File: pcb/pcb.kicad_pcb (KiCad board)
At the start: 2 copper layers, 46 parts, among them J1 Dubugging Headers, J2 Dubugging Headers, SW1 Cherry MX Grey Switch w/ Gree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, SW2 Cherry MX Grey Switch w/ Gree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, SW3 1241.1100.7095, SW4 SW_SPST, U1 Display Driver, U2 Display Driver, U3 MCU, U4 Inverter, 3 Channels, U5 3:8 Demux, U6 NOR, 4 Channels, U7 OR, 2 Channels, U8 5V Buck Voltage Regulator, Y1 20MHz Crystal

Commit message: begin split pcb layout
Signed-off-by: Michael Darr <michael.e.darr@gmail.com>
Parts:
- added C15: 0.1µF, chess_clock:RDER71H104K0M1H03A, F.Cu at (300.2, 42.8)
- added D2: TVS Diode, Diode_SMD:D_SOD-523, F.Cu at (127.3, 205.8)
- added R10: 4.7kΩ, Resistor_THT:R_Axial_DIN0204_L3.6mm_D1.6mm_P2.54mm_Vertical, F.Cu at (285.7, 57.1)
- added R9: 50Ω, chess_clock:352151RFT, F.Cu at (288.5, 49.0)
- J1: value Dubugging Headers -> Debugging; footprint chess_clock:10129381-916001BLF -> Connector_PinHeader_2.54mm:PinHeader_2x16_P2.54mm_Vertical
- J2: value Dubugging Headers -> ISP; footprint chess_clock:10129381-916001BLF -> Connector_PinHeader_2.54mm:PinHeader_2x03_P2.54mm_Vertical
- Y1: value 20MHz Crystal -> 20MHz
- moved U1 233.3 mm to (85.9, 258.7), turned to 90 degrees
- moved C1 198.6 mm to (81.5, 256.2), turned to -90 degrees
- moved U2 193.6 mm to (181.6, 258.7), turned to 90 degrees
- moved R1 187.7 mm to (96.1, 219.3), turned to 180 degrees
- moved R6 173.8 mm to (94.9, 195.0)
- moved SW1 171.7 mm to (92.3, 207.2)
- moved LCD1 151.1 mm to (110.2, 250.8), turned to 90 degrees
- moved LCD2 139.7 mm to (205.8, 250.8), turned to 90 degrees
- moved C7 137.1 mm to (110.5, 210.6), turned to 180 degrees
- moved U3 136.1 mm to (132.5, 205.1)
- moved C2 134.3 mm to (176.8, 256.2), turned to -90 degrees
- moved J1 133.7 mm to (219.7, 16.5)
- moved J2 132.5 mm to (219.7, 24.1)
- moved C3 119.3 mm to (132.5, 198.7), turned to 180 degrees
- moved C14 115.6 mm to (117.3, 205.1), turned to -90 degrees
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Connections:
- C10 pad 2: Net-(BT1-+) -> Net-(U8-VIN)
- C9 pad 1: Net-(BT1-+) -> Net-(U8-VIN)
- J1 pad 10: GND -> digit_2
- J1 pad 11: GND -> digit_1
- J1 pad 12: GND -> data_3
- J1 pad 13: GND -> data_2
- J1 pad 14: GND -> data_1
- J1 pad 15: GND -> data_0
- J1 pad 16: GND -> VCC
- U8 pad 7: Net-(BT1-+) -> Net-(U8-VIN)
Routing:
- net bp: track 0.00 -> 444.6 mm, vias 0 -> 2
- net mux_b: track 0.00 -> 222.0 mm, vias 0 -> 1
- net VCC: track 0.00 -> 218.5 mm, vias 0 -> 1
- net data_0: track 0.00 -> 158.2 mm, vias 0 -> 1
- net data_1: track 0.00 -> 155.1 mm, vias 0 -> 1
- net data_3: track 0.00 -> 154.3 mm, vias 0 -> 1
- net data_2: track 0.00 -> 151.9 mm, vias 0 -> 1
- net digit_1: track 0.00 -> 151.7 mm, vias 0 -> 1
- net digit_2: track 0.00 -> 149.9 mm, vias 0 -> 1
- net /led_1: track 0.00 -> 146.6 mm
- net ~{bp}: track 0.00 -> 128.3 mm, vias 0 -> 1
- net col1: track 0.00 -> 111.0 mm, vias 0 -> 2
- net cs_1_1: track 0.00 -> 109.0 mm, vias 0 -> 1
- net cs_1_2: track 0.00 -> 101.7 mm, vias 0 -> 1
- net /LCD1.G2: track 0.00 -> 90.8 mm
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
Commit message: Separate board halves
Signed-off-by: Michael Darr <michael.e.darr@gmail.com>
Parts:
- moved C6 178.7 mm to (177.1, 206.7)
- moved FET2 140.3 mm to (186.3, 194.5)
- moved C7 82.9 mm to (193.0, 202.6), turned to -90 degrees
- moved U7 77.6 mm to (188.1, 200.9)
- moved U6 76.8 mm to (177.0, 200.1), turned to 180 degrees
- moved C11 57.7 mm to (185.2, 69.7)
- moved C12 57.7 mm to (174.3, 70.2)
- moved C15 57.7 mm to (244.2, 56.4)
- moved C9 57.7 mm to (174.3, 64.3)
- moved J2 57.7 mm to (163.7, 37.8)
- moved LED1 57.7 mm to (110.1, 74.5)
- moved R4 57.7 mm to (210.8, 42.3)
- moved R5 57.7 mm to (210.8, 45.4)
- moved R9 57.7 mm to (232.5, 62.7)
- moved U8 57.7 mm to (130.0, 71.9)
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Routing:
- net ~{col1_enable}: track 2.74 -> 162.6 mm
- net data_3: track 154.3 -> 243.7 mm, vias 1 -> 2
- net ~{sw2_enable}: track 0.00 -> 37.7 mm
- net Net-(FET2-G): track 0.00 -> 36.9 mm
- net ~{bp}: track 128.3 -> 163.2 mm, vias 1 -> 2
- net buzz: track 25.4 -> 56.6 mm
- net GND: track 25.5 -> 0.00 mm
- net cs_1_1: track 109.0 -> 134.0 mm
- net /led_1: track 146.6 -> 170.9 mm
- net ~{sw1_enable}: track 0.00 -> 18.4 mm
- net VCC: track 218.5 -> 235.8 mm
- net col1: track 111.0 -> 127.4 mm
- net ~{sw3_enable}: track 0.00 -> 14.9 mm
- net /sw1∨2_active: track 0.00 -> 12.7 mm
- net sw1_active: track 0.00 -> 11.6 mm
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
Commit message: Finish basic pcb layout
Signed-off-by: Michael Darr <michael.e.darr@gmail.com>
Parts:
- removed J1: Debugging, Connector_PinHeader_2.54mm:PinHeader_2x16_P2.54mm_Vertical
- C1, C10, C11, C15, C2, C3, C4, C5, C6, C7, C8: footprint chess_clock:RDER71H104K0M1H03A -> chess_clock:GRM033R60J104KE19D
- moved R3 180.4 mm to (40.0, 97.3), turned to -90 degrees
- moved R9 175.6 mm to (65.0, 115.3), turned to 90 degrees
- moved R4 175.2 mm to (45.2, 99.8), turned to 90 degrees
- moved FET1 171.3 mm to (36.7, 104.8)
- moved C15 168.0 mm to (89.7, 122.3), turned to 180 degrees
- moved R5 158.6 mm to (72.0, 122.2), turned to 180 degrees
- moved R1 121.2 mm to (47.2, 108.4), turned to 90 degrees
- moved R2 120.1 mm to (154.4, 120.5)
- moved C4 118.6 mm to (134.5, 107.0), turned to 0 degrees
- moved LCD1 116.8 mm to (54.8, 148.0)
- moved LCD2 116.8 mm to (150.5, 148.0)
- moved U1 116.8 mm to (30.6, 155.9)
- moved U2 116.8 mm to (126.2, 155.9)
- moved C7 114.3 mm to (136.0, 103.6)
- moved C12 112.7 mm to (67.5, 106.0), turned to 180 degrees
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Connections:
- net buzz renamed /buzz
- net mux_a renamed /mux_a
- C1 pad 2: VCC -> GND
- C10 pad 1: GND -> Net-(J2-GND)
- C12 pad 1: VCC -> GND
- C2 pad 2: VCC -> GND
- C3 pad 2: VCC -> GND
- C4 pad 1: VCC -> GND
- C5 pad 1: VCC -> GND
- C6 pad 1: VCC -> GND
- C7 pad 1: VCC -> GND
- C7 pad 2: GND -> Net-(J2-GND)
- C9 pad 2: GND -> Net-(J2-GND)
- D2 pad 1: VCC -> GND
- FET1 pad 3: VCC -> GND
- J2 pad 2: VCC -> GND
- J2 pad 6: GND -> Net-(J2-GND)
- L1 pad 1: VCC -> GND
- R10 pad 1: VCC -> GND
- R6 pad 2: VCC -> GND
- R7 pad 2: VCC -> GND
- R8 pad 2: VCC -> GND
- SW3 pad 2: GND -> Net-(J2-GND)
- SW4 pad 1: GND -> Net-(J2-GND)
- U1 pad 1: VCC -> GND
- U2 pad 1: VCC -> GND
- U3 pad 1: VCC -> GND
- U4 pad 8: VCC -> GND
- U5 pad 16: VCC -> GND
- U5 pad 6: VCC -> GND
- U6 pad 14: VCC -> GND
- U6 pad 3: VCC -> GND
- U6 pad 5: VCC -> GND
- U6 pad 9: VCC -> GND
- U7 pad 4: GND -> Net-(J2-GND)
- U7 pad 8: VCC -> GND
- U8 pad 4: VCC -> GND
- U8 pad 5: GND -> Net-(J2-GND)
- U8 pad 6: GND -> Net-(J2-GND)
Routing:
- net GND: track 0.00 -> 574.1 mm, vias 0 -> 5
- net VCC: track 235.8 -> 0.00 mm, vias 1 -> 0
- net Net-(SW1-A): track 7.00 -> 85.4 mm
- net Net-(J2-GND): track 0.00 -> 77.9 mm, vias 0 -> 2
- net Net-(D1-K): track 0.00 -> 72.2 mm
- net Net-(BT1-+): track 0.00 -> 68.9 mm
- net Net-(U8-VIN): track 0.00 -> 58.4 mm
- net Net-(FET1-G): track 0.00 -> 54.7 mm
- net ~{col1_enable}: track 162.6 -> 210.4 mm, vias 0 -> 1
- net Net-(R6-Pad1): track 7.14 -> 49.7 mm
- net /buzz: track 56.6 -> 87.8 mm
- net ~{sw3_enable}: track 14.9 -> 38.7 mm
- net mux_b: track 217.4 -> 193.7 mm
- net Net-(U8-VD): track 0.00 -> 23.1 mm
- net Net-(BT1--): track 0.00 -> 22.6 mm
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
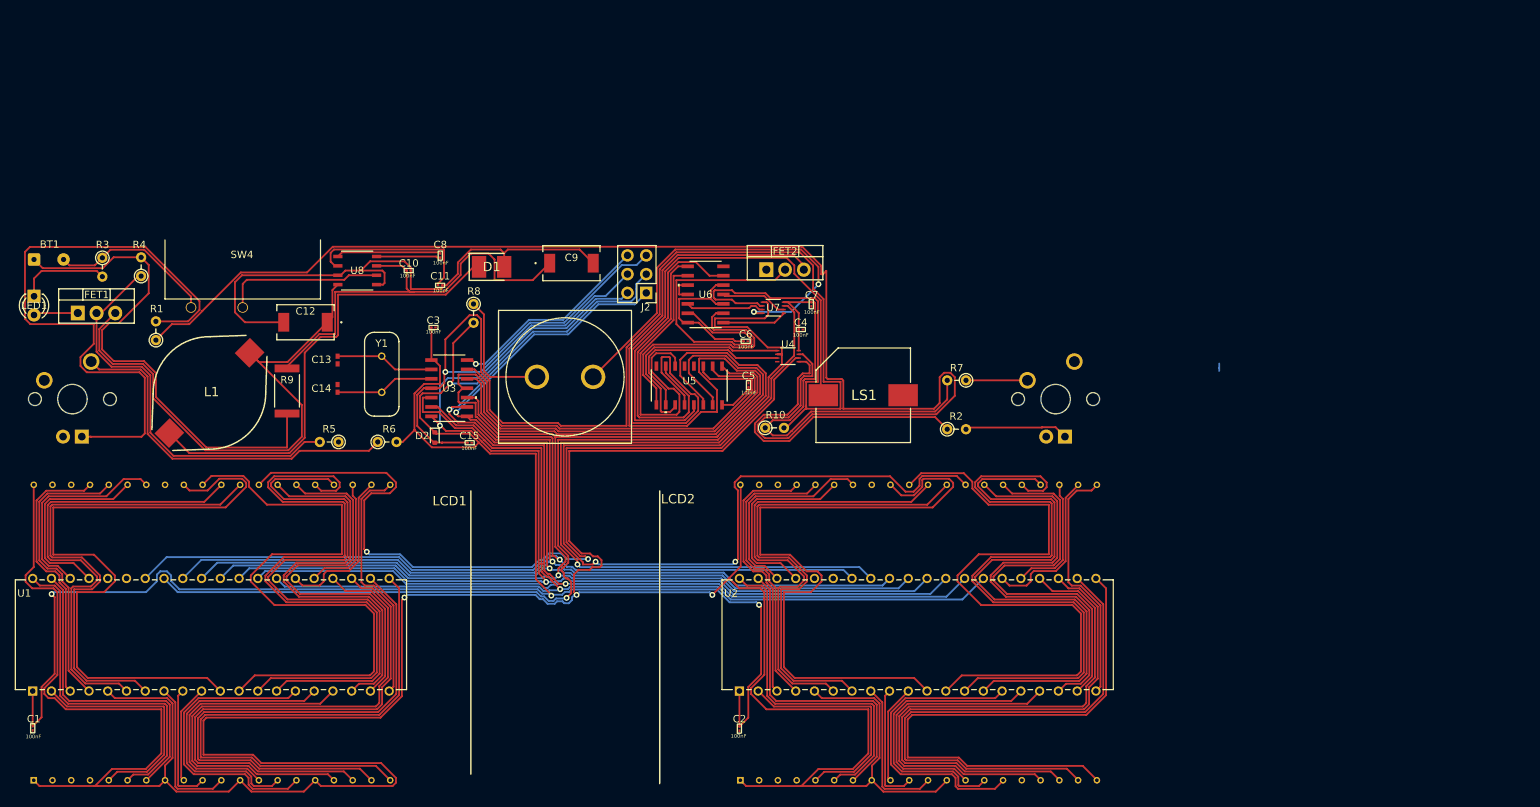
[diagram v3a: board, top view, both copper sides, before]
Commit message: solve solder mask errors
Signed-off-by: Michael Darr <michael.e.darr@gmail.com>
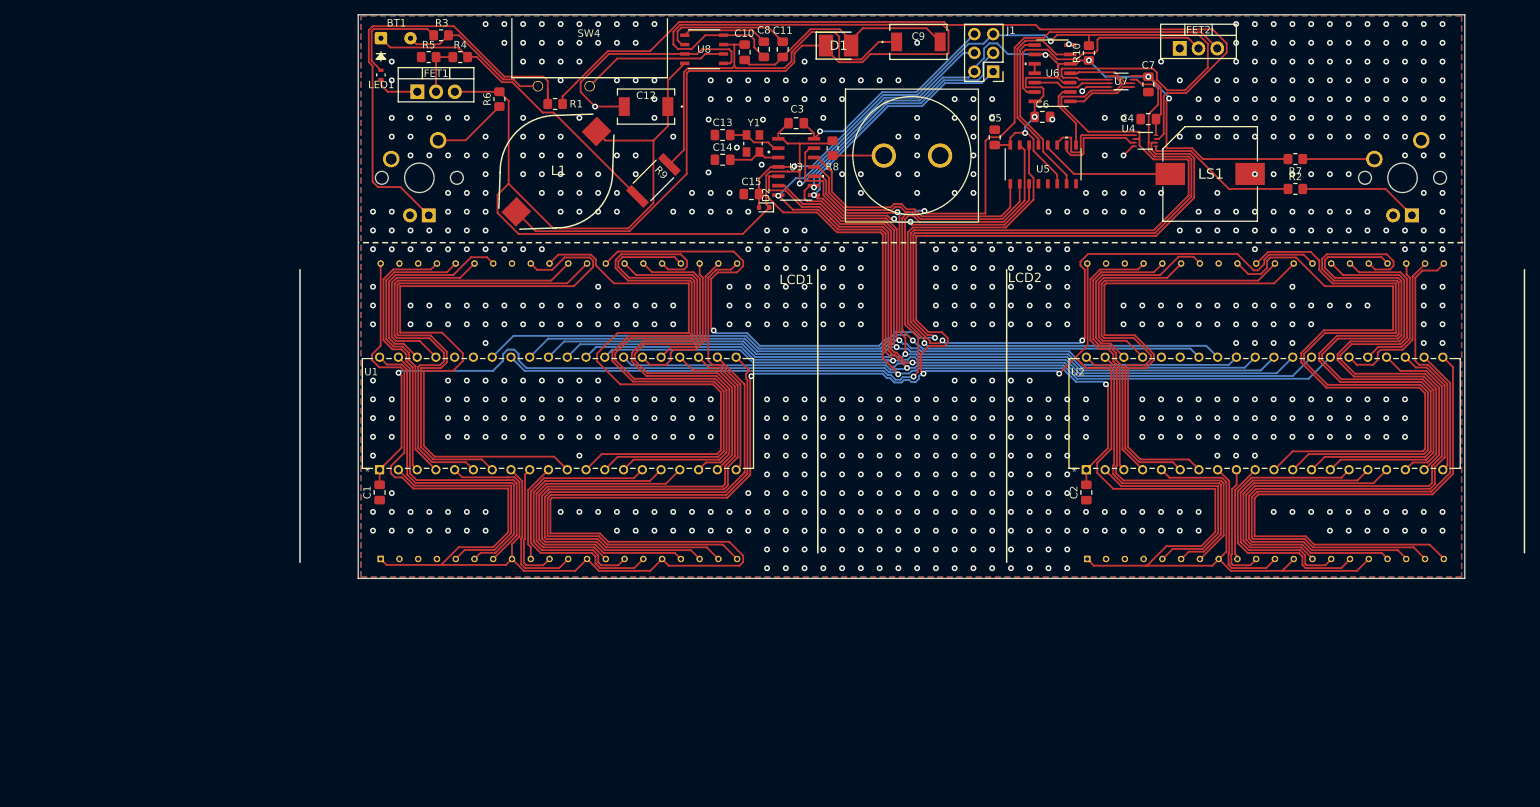
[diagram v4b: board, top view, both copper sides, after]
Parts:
- removed J2: ISP, Connector_PinHeader_2.54mm:PinHeader_2x03_P2.54mm_Vertical
- added J1: ISP, Connector_PinHeader_2.54mm:PinHeader_2x03_P2.54mm_Vertical, F.Cu at (160.6, 72.1)
- C1, C10, C11, C15, C2, C3, C4, C5, C6, C7, C8: footprint chess_clock:GRM033R60J104KE19D -> Capacitor_SMD:C_0805_2012Metric_Pad1.18x1.45mm_HandSolder
- C13, C14: value 11pF -> 22pF; footprint chess_clock:GJM1555C1H110FB01D -> Capacitor_SMD:C_0805_2012Metric_Pad1.18x1.45mm_HandSolder
- LED1: footprint LED_THT:LED_D3.0mm_Clear -> chess_clock:150060RS75000
- R1, R10, R2, R3, R4, R5, R6, R7, R8: footprint Resistor_THT:R_Axial_DIN0204_L3.6mm_D1.6mm_P2.54mm_Vertical -> Resistor_SMD:R_0805_2012Metric_Pad1.20x1.40mm_HandSolder
- Y1: footprint chess_clock:ECS_200_18_4X_CKM -> chess_clock:ABM8-20.000MHZ-10-B1U-T
- moved R10 67.0 mm to (173.6, 69.5), turned to 90 degrees
- moved FET2 63.5 mm to (185.8, 68.9)
- moved R1 62.8 mm to (101.3, 76.5), turned to 180 degrees
- moved C14 60.6 mm to (124.0, 84.0), turned to 0 degrees
- moved C13 60.4 mm to (124.0, 80.7), turned to 0 degrees
- moved Y1 59.2 mm to (128.1, 81.8), turned to 180 degrees
- moved R2 57.3 mm to (201.5, 88.0)
- moved R9 57.2 mm to (114.6, 86.8), turned to 45 degrees
- moved C2 56.8 mm to (173.2, 129.0)
- moved C1 56.8 mm to (77.5, 129.0)
- moved U5 56.5 mm to (167.4, 84.6), turned to 90 degrees
- moved U4 56.5 mm to (181.2, 81.4)
- moved C3 56.3 mm to (133.9, 79.0)
- moved C11 56.3 mm to (132.1, 69.1), turned to 90 degrees
- moved U7 56.2 mm to (177.9, 73.4)
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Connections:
- C1 pad 2: GND -> VCC
- C10 pad 1: Net-(J2-GND) -> GND
- C12 pad 1: GND -> VCC
- C2 pad 2: GND -> VCC
- C3 pad 2: GND -> VCC
- C4 pad 1: GND -> VCC
- C5 pad 1: GND -> VCC
- C6 pad 1: GND -> VCC
- C7 pad 1: GND -> VCC
- C7 pad 2: Net-(J2-GND) -> GND
- C9 pad 2: Net-(J2-GND) -> GND
- D2 pad 1: GND -> VCC
- FET1 pad 3: GND -> VCC
- L1 pad 1: GND -> VCC
- R10 pad 1: GND -> VCC
- R6 pad 2: GND -> VCC
- R7 pad 2: GND -> VCC
- R8 pad 2: GND -> VCC
- SW3 pad 2: Net-(J2-GND) -> GND
- SW4 pad 1: Net-(J2-GND) -> GND
- U1 pad 1: GND -> VCC
- U2 pad 1: GND -> VCC
- U3 pad 1: GND -> VCC
- U4 pad 8: GND -> VCC
- U5 pad 16: GND -> VCC
- U5 pad 6: GND -> VCC
- U6 pad 14: GND -> VCC
- U6 pad 3: GND -> VCC
- U6 pad 5: GND -> VCC
- U6 pad 9: GND -> VCC
- U7 pad 4: Net-(J2-GND) -> GND
- U7 pad 8: GND -> VCC
- U8 pad 4: GND -> VCC
- U8 pad 5: Net-(J2-GND) -> GND
- U8 pad 6: Net-(J2-GND) -> GND
- Y1 pad 2: Net-(U3-(PCINT8/XTAL1/CLKI)_PB0) -> GND
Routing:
- net GND: track 574.1 -> 119.3 mm, vias 5 -> 816
- net VCC: track 0.00 -> 443.8 mm, vias 0 -> 10
- net ~{col1_enable}: track 210.4 -> 109.2 mm, vias 1 -> 2
- net Net-(J2-GND): track 77.9 -> 0.00 mm, vias 2 -> 0
- net /led_1: track 187.7 -> 115.0 mm
- net /buzz: track 87.8 -> 18.4 mm
- net Net-(D1-K): track 72.2 -> 138.3 mm
- net Net-(FET1-G): track 54.7 -> 6.97 mm
- net data_3: track 241.2 -> 200.0 mm, vias 1 -> 3
- net mux_b: track 193.7 -> 153.7 mm
- net Net-(R6-Pad1): track 49.7 -> 10.2 mm
- net cs_1_2: track 111.8 -> 82.9 mm
- net bp: track 441.2 -> 469.0 mm
- net cs_1_1: track 131.1 -> 104.0 mm
- net Net-(BT1-+): track 68.9 -> 43.3 mm
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- added copper zone on B.Cu, net GND
- added copper zone on F.Cu, net GND
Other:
- board outline added: 149.8 x 76.3 mm
- rule pad_to_mask_clearance: 2 -> 0.038
- board text added: "0.1.0"

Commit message: Prepare for connection
Signed-off-by: Michael Darr <michael.e.darr@gmail.com>
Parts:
- added J2: Ribbon Cable Header, chess_clock:903250014, F.Cu at (148.5, 152.5)
- added J3: ISP, Connector_PinHeader_2.54mm:PinHeader_2x03_P2.54mm_Vertical, F.Cu at (160.6, 72.1)
- J1: value ISP -> Ribbon Cable Header; footprint Connector_PinHeader_2.54mm:PinHeader_2x03_P2.54mm_Vertical -> chess_clock:903250014
- moved J1 96.3 mm to (254.9, 91.5)
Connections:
- J1 pad 1: digit_2 -> col1
- J1 pad 2: VCC -> ~{bp}
- J1 pad 3: digit_1 -> cs_1_2
- J1 pad 4: data_2 -> mux_b
- J1 pad 5: ~{col1_enable} -> digit_2
- J1 pad 6: GND -> digit_1

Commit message: crush every error
Signed-off-by: Michael Darr <michael.e.darr@gmail.com>
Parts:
- SW1, SW2: value Cherry MX Grey Switch w/ Green LED -> MX Grey w/ LED
- moved J1 84.1 mm to (170.8, 89.9)
- moved J2 54.8 mm to (148.7, 97.7)
- moved J3 4.57 mm to (156.5, 70.0)
- moved C9 3.89 mm to (147.1, 66.0)
- moved R9 3.70 mm to (114.6, 83.1), turned to 0 degrees
- moved D1 2.14 mm to (138.9, 66.5)
- moved BT1 2.00 mm to (77.7, 65.5)
- moved C10 2.00 mm to (127.0, 67.5)
- moved C11 2.00 mm to (132.1, 67.1)
- moved C13 2.00 mm to (124.0, 78.7)
- moved C14 2.00 mm to (124.0, 82.0)
- moved C15 2.00 mm to (127.9, 86.7)
- moved C3 2.00 mm to (133.9, 77.0)
- moved C4 2.00 mm to (181.6, 76.5)
- moved C5 2.00 mm to (160.8, 79.0)
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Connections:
- C1 pad 1: GND -> VSS
- C1 pad 2: VCC -> VDD
- C2 pad 1: GND -> VSS
- C2 pad 2: VCC -> VDD
- J1 pad 1: col1 -> col1_bp
- J1 pad 11: VCC -> lcd_bp
- J1 pad 12: cs_1_1 -> lcd2_write
- J1 pad 13: bp -> GND
- J1 pad 14: GND -> ~{lcd_bp}
- J1 pad 2: ~{bp} -> VCC
- J1 pad 3: cs_1_2 -> mux_b
- J1 pad 4: mux_b -> lcd1_write
- J2 pad 10: data_0 -> d0
- J2 pad 11: VCC -> bp
- J2 pad 12: cs_1_1 -> cs_1_2
- J2 pad 13: bp -> VSS
- J2 pad 14: GND -> ~{bp}
- J2 pad 2: ~{bp} -> VDD
- J2 pad 3: cs_1_2 -> cs_2
- J2 pad 4: mux_b -> cs_1_1
- J2 pad 5: digit_2 -> ds_2
- J2 pad 6: digit_1 -> ds_1
- J2 pad 7: data_3 -> d3
- J2 pad 8: data_2 -> d2
- J2 pad 9: data_1 -> d1
- U1 pad 1: VCC -> VDD
- U1 pad 27: data_0 -> d0
- U1 pad 28: data_1 -> d1
- U1 pad 29: data_2 -> d2
- U1 pad 30: data_3 -> d3
- U1 pad 31: digit_1 -> ds_1
- U1 pad 32: digit_2 -> ds_2
- U1 pad 34: mux_b -> cs_2
- U1 pad 35: GND -> VSS
- U2 pad 1: VCC -> VDD
- U2 pad 27: data_0 -> d0
- U2 pad 28: data_1 -> d1
- U2 pad 29: data_2 -> d2
- U2 pad 30: data_3 -> d3
- U2 pad 31: digit_1 -> ds_1
- U2 pad 32: digit_2 -> ds_2
- U2 pad 34: mux_b -> cs_2
- U2 pad 35: GND -> VSS
- U2 pad 36: GND -> VSS
- U4 pad 2: ~{bp} -> ~{lcd_bp}
- U4 pad 6: bp -> lcd_bp
- U5 pad 14: cs_1_2 -> lcd2_write
- U5 pad 15: cs_1_1 -> lcd1_write
- U7 pad 1: ~{bp} -> ~{lcd_bp}
- U7 pad 7: col1 -> col1_bp
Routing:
- net VDD: track 0.00 -> 173.2 mm
- net VCC: track 443.8 -> 276.5 mm, vias 10 -> 9
- net ~{bp}: track 161.3 -> 47.5 mm, vias 2 -> 0
- net d0: track 0.00 -> 111.2 mm
- net d2: track 0.00 -> 110.8 mm
- net ds_1: track 0.00 -> 110.8 mm
- net d1: track 0.00 -> 105.6 mm
- net d3: track 0.00 -> 105.6 mm
- net ds_2: track 0.00 -> 105.4 mm
- net cs_2: track 0.00 -> 105.4 mm
- net col1: track 144.1 -> 38.8 mm, vias 2 -> 0
- net mux_b: track 153.7 -> 49.1 mm, vias 1 -> 0
- net data_0: track 139.8 -> 43.7 mm, vias 1 -> 0
- net data_1: track 136.6 -> 41.2 mm, vias 1 -> 0
- net data_2: track 167.9 -> 72.6 mm, vias 2 -> 1
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- added copper zone on B.Cu, net VSS
- added copper zone on F.Cu, net VSS
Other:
- board size 149.8 x 76.3 mm -> 149.7 x 78 mm

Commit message: Add some snazy art
Signed-off-by: Michael Darr <michael.e.darr@gmail.com>
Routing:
- net Net-(SW1-A): track 62.6 -> 60.6 mm
- net /LCD2.A2: track 99.9 -> 99.4 mm
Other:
- board text added: "liclock"
- board text added: "╔════════╗ ║ ║ ╚════════╝ ┏━⬓━━▬━━⬓━ ┌─────┚ ▝███▖▜██▙ │╲ ┗━━━━━━━━━━┛ │ ╒═════╤═══════════╕ │╲│ REV │ 0.1.0 │ │ ├─────┼───────────┤ ╵╲│ MFR │ JLCPCB │ ├─────┴───────────┤"
- board text removed: "0.1.0"

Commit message: Add mouse bites
Signed-off-by: Michael Darr <michael.e.darr@gmail.com>
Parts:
- moved R3 1.50 mm to (85.8, 63.6)
- moved BT1 1.50 mm to (77.7, 64.0)
- moved C10 1.50 mm to (127.0, 66.0)
- moved C11 1.50 mm to (132.1, 65.6)
- moved C12 1.50 mm to (115.1, 74.3)
- moved C13 1.50 mm to (124.0, 77.2)
- moved C14 1.50 mm to (124.0, 80.5)
- moved C15 1.50 mm to (127.9, 85.2)
- moved C3 1.50 mm to (133.9, 75.5)
- moved C4 1.50 mm to (181.6, 75.0)
- moved C5 1.50 mm to (160.8, 77.5)
- moved C6 1.50 mm to (167.2, 74.7)
- moved C7 1.50 mm to (181.6, 70.3)
- moved C8 1.50 mm to (129.6, 65.5)
- moved C9 1.50 mm to (147.1, 64.5)
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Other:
- board size 149.7 x 78 mm -> 149.6 x 79.8 mm
- board text added: "╔════════╗ ║ ║ ╚════════╝ ┏━⬓━━▬━━⬓━. ┌──┚`▝███▖▜██▙`ˎ─. │╲ ꞌ━━━━━━━━━┙ ╲ │ ╒═════╤══════════╕ │╲│ REV │ 0.1.0 │ │ ├─────┼──────────┤ ╵╲│ MFR │ JLCPCB │ ├─────┴──────────┤"
- board text added: "♙"
- board text added: "♟"
- board text removed: "╔════════╗ ║ ║ ╚════════╝ ┏━⬓━━▬━━⬓━ ┌─────┚ ▝███▖▜██▙ │╲ ┗━━━━━━━━━━┛ │ ╒═════╤═══════════╕ │╲│ REV │ 0.1.0 │ │ ├─────┼───────────┤ ╵╲│ MFR │ JLCPCB │ ├─────┴───────────┤"
